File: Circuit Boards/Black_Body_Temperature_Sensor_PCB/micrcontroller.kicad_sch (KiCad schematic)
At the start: 30 parts, among them J701 Conn_01x06_Pin, J702 5040500891, J703 USB_C_Receptacle_USB2.0_16P, J704 Conn_01x04_Pin, P701 pogo programmer, SW701 SW_MEC_5E, SW702 SW_MEC_5E, U701 TXU0304, U702 ABM8G-25.000MHZ-18-D2Y-T, U703 USBLC6-2SC6, U704 STM32G431RBTx, U705 AMS1117-3.3

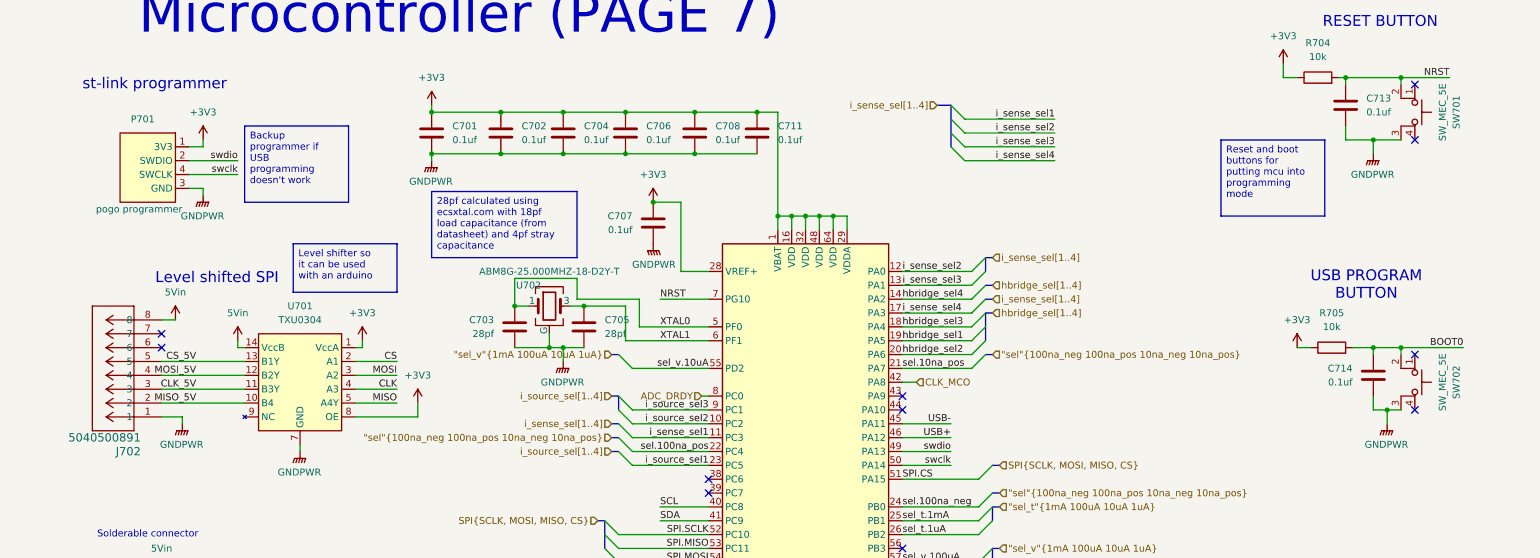
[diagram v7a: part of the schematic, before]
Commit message: Temp probe bom done
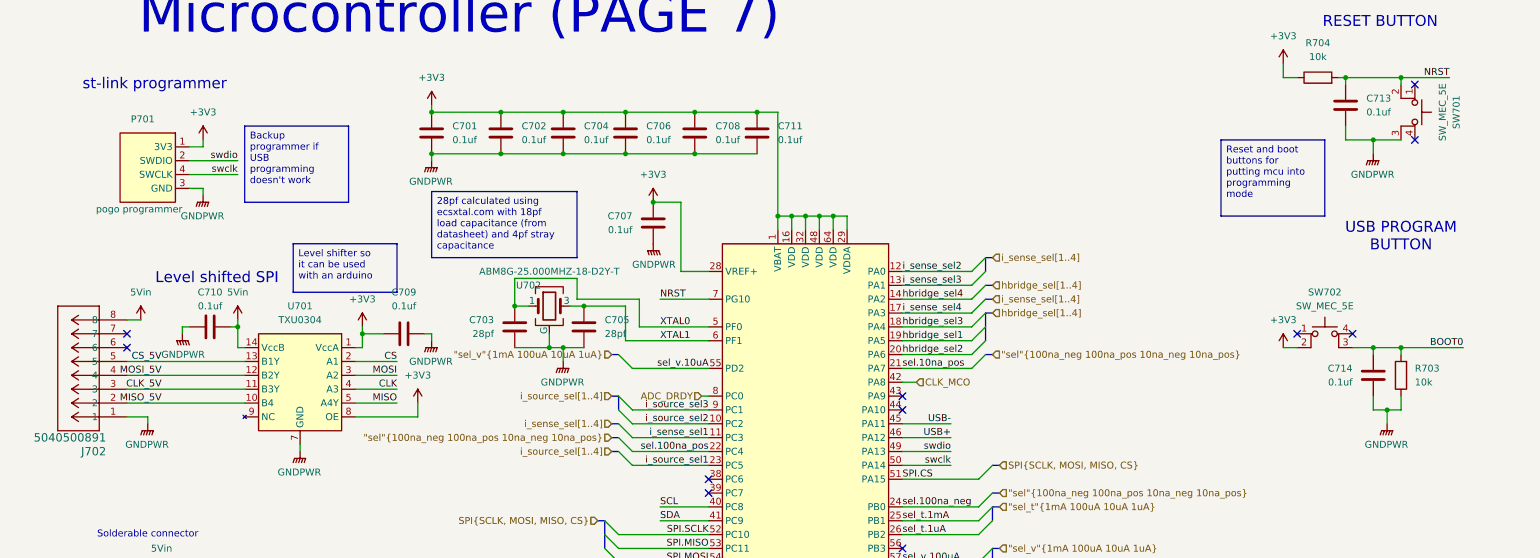
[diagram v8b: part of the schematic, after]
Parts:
- removed R705: 10k, Resistor_SMD:R_0603_1608Metric, symbol Device:R
- added C709, C710: 0.1uf, Capacitor_SMD:C_0603_1608Metric, symbol Device:C
- added R703: 10k, Resistor_SMD:R_0603_1608Metric, symbol Device:R
- C701, C702, C704, C706, C707, C708, C711, C713, C714: MPN (none) -> CL10B104KB8NNNC
- C703, C705: MPN (none) -> CL10C270JB8NNNC
- C712: MPN (none) -> GRM188R6YA106MA73D
- C715: MPN (none) -> CL10A226MP8NUNE
- D701: MPN (none) -> 1N5819WS
- J702: MPN (none) -> 5040500891
- J703: MPN (none) -> UJ20-C-H-G-SMT-1-P16-TR
- R701, R702: MPN (none) -> RT0402BRD075K1L
- R704: MPN (none) -> ERA-3AEB103V
- SW701, SW702: MPN (none) -> 430471035826
- U701: MPN (none) -> TXU0304
- U702: MPN (none) -> ABM8G-25.000MHZ-18-D2Y-T
- U703: MPN (none) -> USBLC6-2SC6c
- U704: MPN (none) -> STM32G431RBT6
- U705: MPN (none) -> AMS1117-3.3
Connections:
- net +3V3: now also SW702.2, C709.1
- net 5Vin: now also C710.1
- net BOOT0: now also SW702.3 (K), R703.2; no longer SW702.2
- net GNDPWR: now also C709.2, C710.2, R703.1; no longer SW702.3 (K)
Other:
- moved on the sheet: J702
